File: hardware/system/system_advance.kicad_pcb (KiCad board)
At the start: 2 copper layers, 121.1 x 172.7 mm, 45 parts, among them J1 CART_SOCKET_28P, J2 EXTENSION PINS, SW1 POWER, SW2 RESET, SW3 A, SW4 B, SW5 UP, SW6 DN, SW7 LF, SW8 RT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

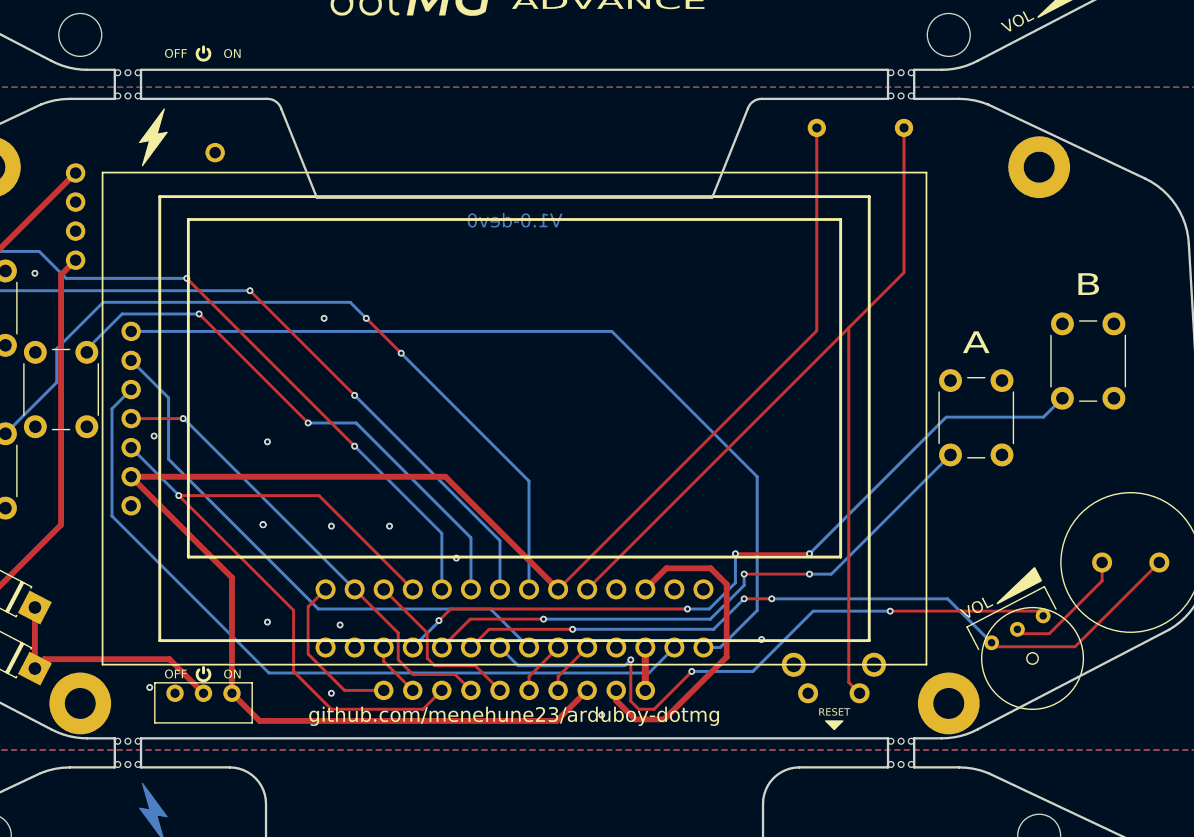
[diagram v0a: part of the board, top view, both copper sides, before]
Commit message: Minor board updates
- Add logo to main board
- Increase breakaway tab width (better for fabs)
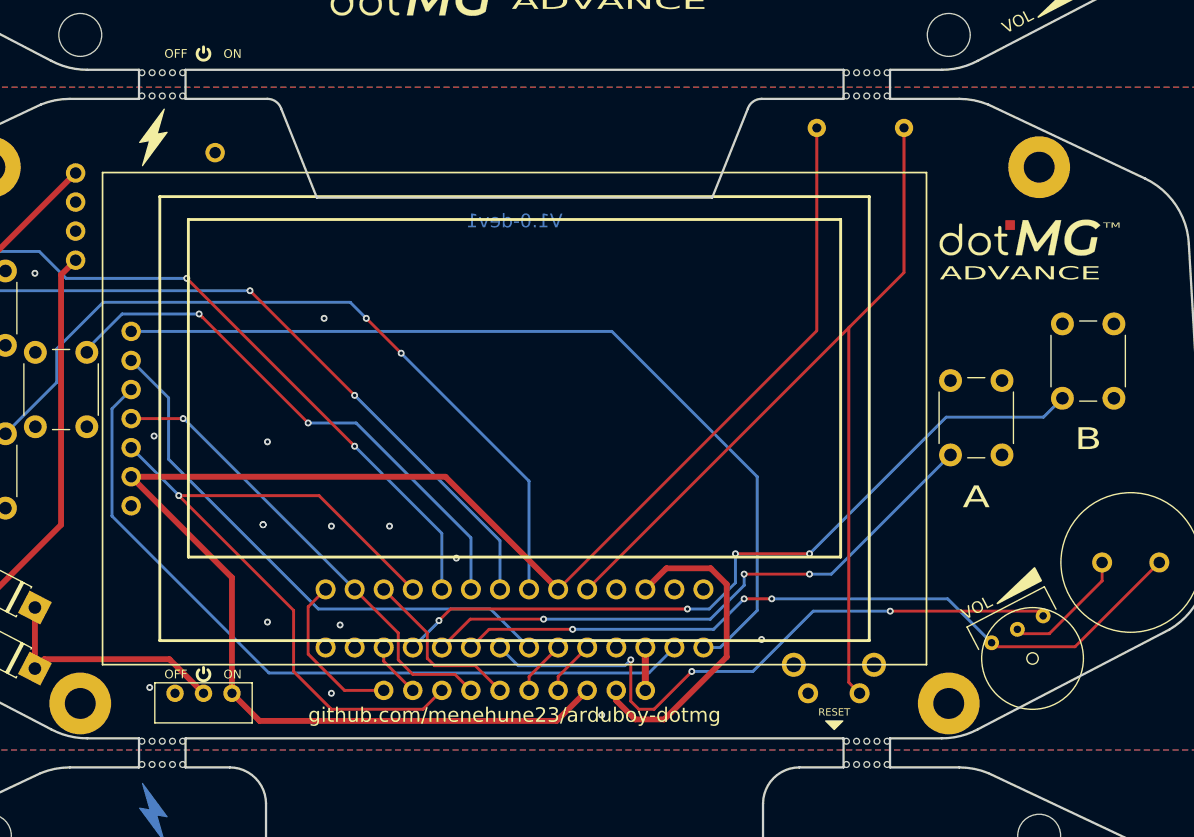
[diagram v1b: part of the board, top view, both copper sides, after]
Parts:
- added G***: LOGO, system:LOGO, F.Cu at (151.3, 122.8)
- moved REF** 3.00 mm to (138.7, 111.8)
- moved REF** 3.00 mm to (77.2, 170.2)
- moved REF** 3.00 mm to (138.7, 170.2)
- moved REF** 3.00 mm to (77.2, 111.8)
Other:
- outline, holes or cut-outs redrawn
- board text added: "V1.0-dev1"
- board text removed: "V1.0-dev0"
